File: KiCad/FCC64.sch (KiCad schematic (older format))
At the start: 1 part

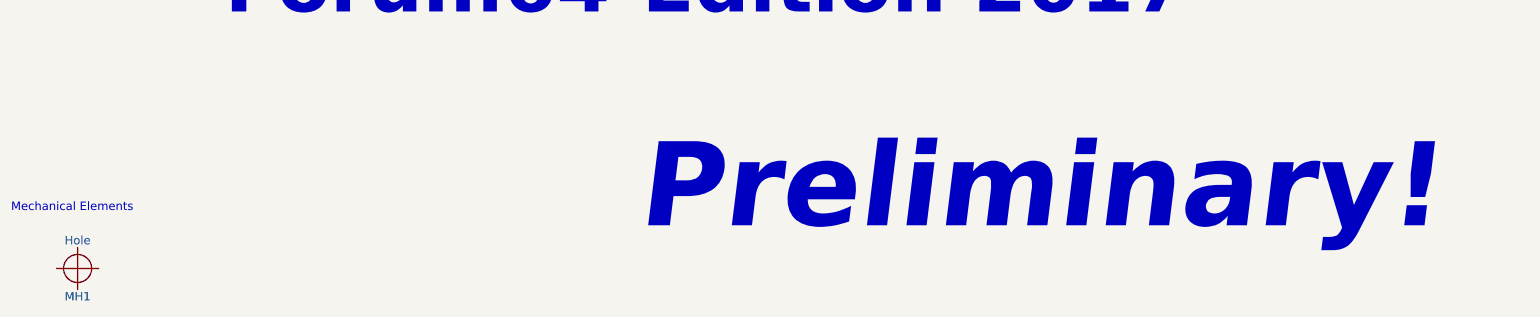
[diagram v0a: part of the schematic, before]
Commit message: Various issues solved:
* QFP44-Footprint for W65C02 corrected
* FCC-On/Off deleted
* new battery supervisor ic TPS6513-01
* Battery Holder corrected
* Signals D5 and D7 to CPLD swapped
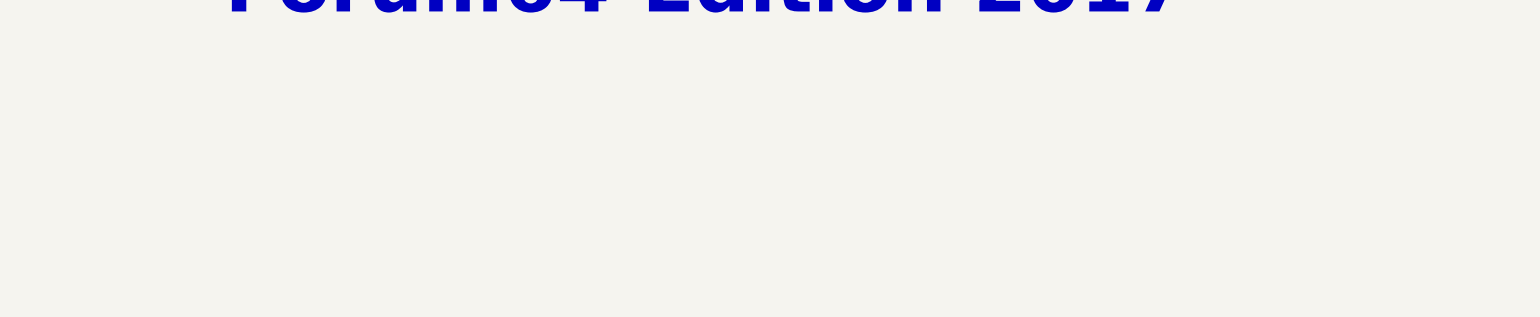
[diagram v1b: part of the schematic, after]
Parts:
- removed MH1: Hole, TTB_MyLib:TTB_Hole3,2mm, symbol Hole
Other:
- note removed: "Mechanical Elements"
- note removed: "Preliminary!"
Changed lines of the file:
@@
 Sheet 1 3
 Title "The Final Chesscard (Forum64-Edition 2017)"
-Date "2017-05-04"
-Rev "-"
+Date "2017-07-09"
+Rev "1.0"
 Comp ""
 Comment1 ""
@@
 Text Notes 2550 5600 0    400  ~ 80
 Forum64-Edition 2017\n
-$Comp
-L Hole MH1
-U 1 1 590A61BD
-P 1500 7375
-F 0 "MH1" H 1500 7175 60  0000 C CNN
-F 1 "Hole" H 1500 7575 60  0000 C CNN
-F 2 "TTB_MyLib:TTB_Hole3,2mm" H 1500 7375 60  0001 C CNN
-F 3 "" H 1500 7375 60  0000 C CNN
-	1    1500 7375
-	1    0    0    -1
-$EndComp
-Text Notes 1025 6975 0    60   ~ 0
-Mechanical Elements
-Text Notes 11225 7150 2    600  Italic 120
-Preliminary!
 $EndSCHEMATC
